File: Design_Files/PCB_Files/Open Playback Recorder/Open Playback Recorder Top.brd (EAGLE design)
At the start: 100 x 30 mm, 18 parts

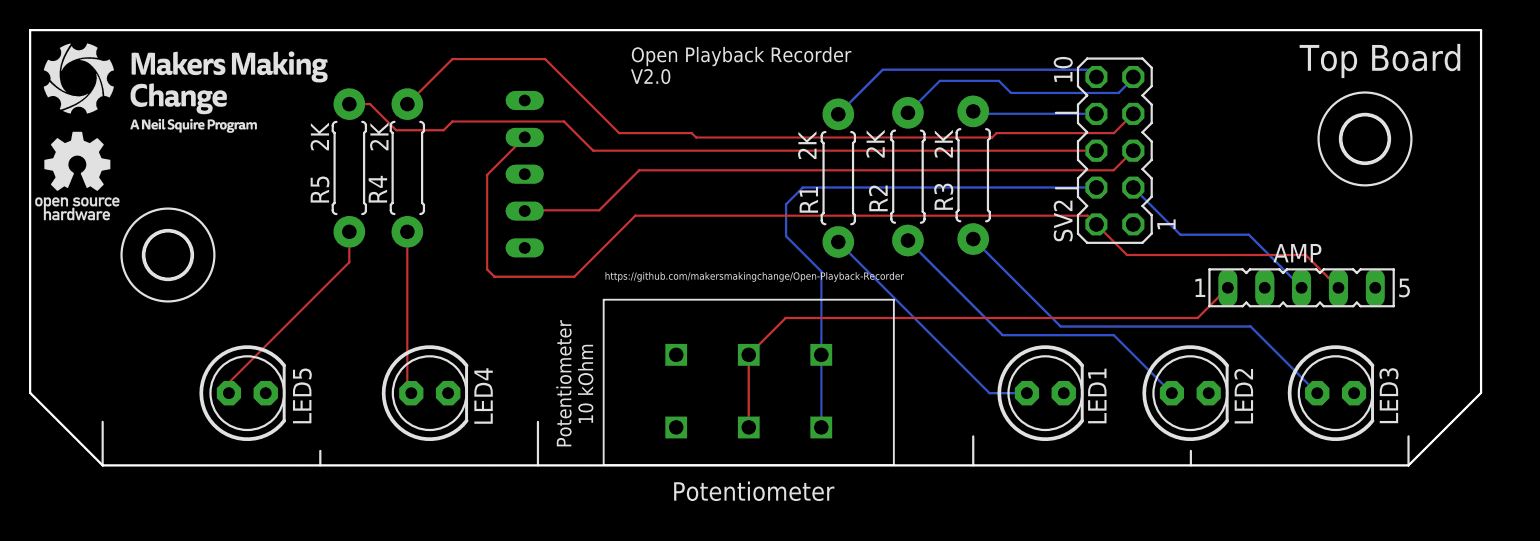
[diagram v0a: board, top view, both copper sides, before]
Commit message: Updated files with OSHWA Certification
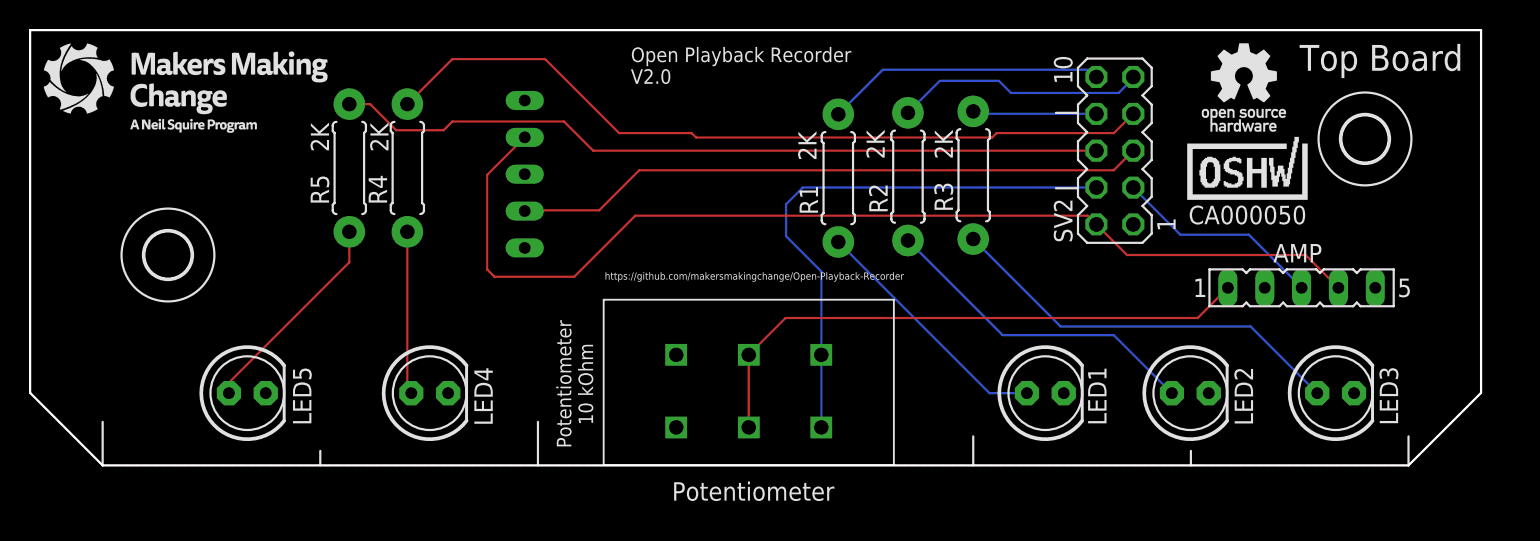
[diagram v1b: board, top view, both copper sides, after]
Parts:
- added U$4: CA000050, MMC_Eagle:OSHWA-CERT-SMALL-SILK
- moved U$3 80.6 mm to (83.6, 26.0)
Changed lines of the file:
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@@
 </element>
 <element name="U$1" library="MMC_Eagle" library_urn="urn:adsk.eagle:library:44377252" package="MMC_SMALL_LOGO" package3d_urn="urn:adsk.eagle:package:44377666/1" value="" x="12" y="26" smashed="yes"/>
-<element name="U$3" library="MMC_Eagle" library_urn="urn:adsk.eagle:library:44377252" package="OSHW_X-SMALL_LOGO" package3d_urn="urn:adsk.eagle:package:44377679/1" value="" x="3.2" y="19.9" smashed="yes"/>
+<element name="U$3" library="MMC_Eagle" library_urn="urn:adsk.eagle:library:44377252" package="OSHW_X-SMALL_LOGO" package3d_urn="urn:adsk.eagle:package:44377679/1" value="" x="83.6" y="26" smashed="yes"/>
+<element name="U$4" library="MMC_Eagle" library_urn="urn:adsk.eagle:library:44377252" package="OSHWA-CERT-SMALL-SILK" package3d_urn="urn:adsk.eagle:package:44378011/1" value="CA000050" x="83.9" y="18.3" smashed="yes">
+<attribute name="VALUE" x="79.83005625" y="16.622" size="1.27" layer="21" font="vector" ratio="12"/>
+</element>
 </elements>
 <signals>
